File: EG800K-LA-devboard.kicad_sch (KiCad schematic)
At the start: 37 parts, among them J1 U.FL-R-SMT_10_, J2 MICROQTJ, J4 Conn_01x11_Pin, Q1 DTC143ZUAT106, Q2 DTC143ZUAT106, Q4 DTC143ZUAT106, Q5 DTC143ZUAT106, U1 EG800KEULC-I03-SNNSA

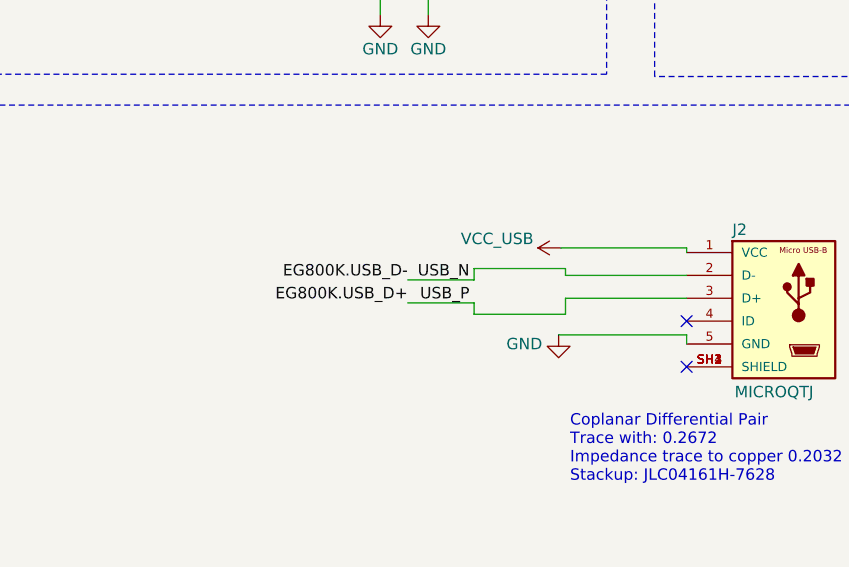
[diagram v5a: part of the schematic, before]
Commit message: Agregados res en serie en USB
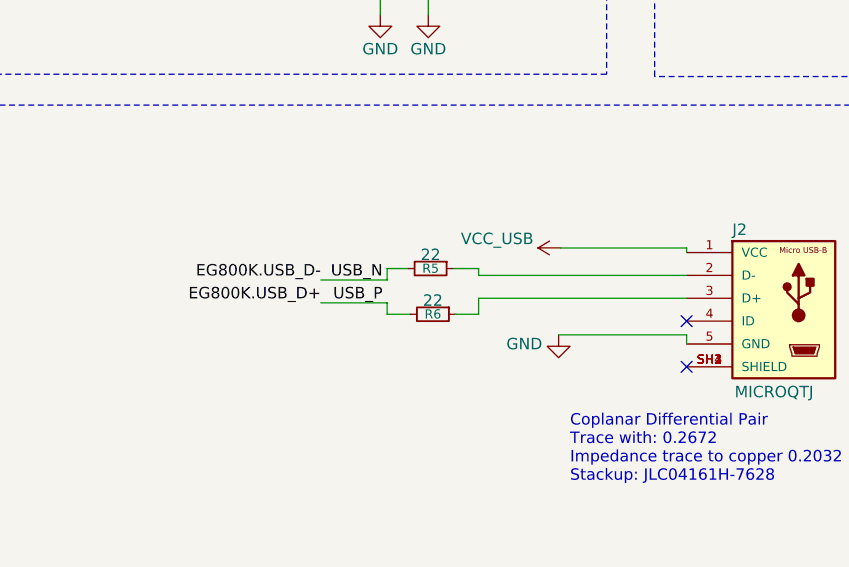
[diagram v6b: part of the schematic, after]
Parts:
- added R5, R6: 22, Resistor_SMD:R_0201_0603Metric_Pad0.64x0.40mm_HandSolder, symbol Device:R_Small
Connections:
- net EG800K.USB_D+: now also R6.2; no longer J2.3 (D+)
- net EG800K.USB_D-: now also R5.2; no longer J2.2 (D-)
- new net: J2.2 (D-), R5.1
- new net: J2.3 (D+), R6.1
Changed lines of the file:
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@@
 	(wire
 		(pts
-			(xy 105.664 174.752) (xy 119.126 174.752)
+			(xy 96.012 174.752) (xy 119.126 174.752)
 		)
 		(stroke
@@
 	(wire
 		(pts
-			(xy 88.138 175.26) (xy 95.504 175.26)
+			(xy 78.486 175.26) (xy 85.852 175.26)
 		)
 		(stroke
@@
 	(wire
 		(pts
-			(xy 95.504 177.8) (xy 95.504 179.07)
+			(xy 85.852 177.8) (xy 85.852 179.07)
 		)
 		(stroke
@@
 	(wire
 		(pts
-			(xy 88.138 177.8) (xy 95.504 177.8)
+			(xy 78.486 177.8) (xy 85.852 177.8)
 		)
 		(stroke
@@
 	(wire
 		(pts
-			(xy 95.504 175.26) (xy 95.504 173.99)
+			(xy 85.852 175.26) (xy 85.852 173.99)
 		)
 		(stroke
@@
 	(wire
 		(pts
-			(xy 95.504 179.07) (xy 105.664 179.07)
+			(xy 85.852 179.07) (xy 88.392 179.07)
 		)
 		(stroke
@@
 	(wire
 		(pts
+			(xy 93.218 173.99) (xy 96.012 173.99)
+		)
+		(stroke
+			(width 0)
+			(type default)
+		)
+	)
+	(wire
+		(pts
 			(xy 271.78 76.454) (xy 269.24 76.454)
 		)
@@
 	(wire
 		(pts
-			(xy 95.504 173.99) (xy 105.664 173.99)
+			(xy 85.852 173.99) (xy 88.138 173.99)
 		)
 		(stroke
@@
 	(wire
 		(pts
-			(xy 105.664 179.07) (xy 105.664 177.292)
+			(xy 96.012 179.07) (xy 96.012 177.292)
 		)
 		(stroke
@@
 	(wire
 		(pts
-			(xy 105.664 173.99) (xy 105.664 174.752)
+			(xy 96.012 173.99) (xy 96.012 174.752)
 		)
 		(stroke
@@
 	(wire
 		(pts
-			(xy 105.664 177.292) (xy 119.126 177.292)
+			(xy 96.012 177.292) (xy 119.126 177.292)
 		)
 		(stroke
@@
 	(wire
 		(pts
+			(xy 93.472 179.07) (xy 96.012 179.07)
+		)
+		(stroke
+			(width 0)
+			(type default)
+		)
+	)
+	(wire
+		(pts
 			(xy 39.624 272.288) (xy 53.086 272.288)
 		)
@@
 	)
 	(label "USB_N"
-		(at 94.996 175.26 180)
+		(at 85.344 175.26 180)
 		(effects
 			(font
@@
 	)
 	(label "USB_P"
-		(at 94.996 177.8 180)
+		(at 85.344 177.8 180)
 		(effects
 			(font
@@
 	)
 	(label "EG800K.USB_D+"
-		(at 88.138 177.8 180)
+		(at 78.486 177.8 180)
 		(effects
 			(font
@@
 	)
 	(label "EG800K.USB_D-"
-		(at 88.138 175.26 180)
+		(at 78.486 175.26 180)
 		(effects
 			(font
@@
 					(unit 1)
 				)
+			)
+		)
+	)
+	(symbol
+		(lib_name "R_Small_1")
+		(lib_id "Device:R_Small")
+		(at 90.932 179.07 270)
+		(unit 1)
+		(exclude_from_sim no)
+		(in_bom yes)
+		(on_board yes)
+		(dnp no)
+		(property "Reference" "R6"
+			(at 90.932 179.07 90)
+			(effects
+				(font
+					(size 1.016 1.016)
+				)
+			)
+		)
+		(property "Value" "22"
+			(at 90.932 177.546 90)
+			(effects
+				(font
+					(size 1.27 1.27)
+				)
+			)
+		)
+		(property "Footprint" "Resistor_SMD:R_0201_0603Metric_Pad0.64x0.40mm_HandSolder"
+			(at 90.932 179.07 0)
+			(effects
+				(font
+					(size 1.27 1.27)
+				)
+				(hide yes)
+			)
+		)
+		(property "Datasheet" "~"
+			(at 90.932 179.07 0)
+			(effects
+				(font
+					(size 1.27 1.27)
+				)
+				(hide yes)
+			)
+		)
+		(property "Description" "Resistor, small symbol"
+			(at 90.932 179.07 0)
+			(effects
+				(font
+					(size 1.27 1.27)
+				)
+				(hide yes)
+			)
+		)
+		(pin "1"
+		)
+		(pin "2"
+		)
+		(instances
+			(project "EG800K-LA-devboard"
+				(path "/1dd4973b-ee9b-455c-8ac7-91801682b6f0"
+					(reference "R6")
+					(unit 1)
+				)
+			)
+		)
+	)
+	(symbol
+		(lib_name "R_Small_1")
+		(lib_id "Device:R_Small")
+		(at 90.678 173.99 270)
+		(unit 1)
+		(exclude_from_sim no)
+		(in_bom yes)
+		(on_board yes)
+		(dnp no)
+		(property "Reference" "R5"
+			(at 90.678 173.99 90)
+			(effects
+				(font
+					(size 1.016 1.016)
+				)
+			)
+		)
+		(property "Value" "22"
+			(at 90.678 172.466 90)
+			(effects
+				(font
+					(size 1.27 1.27)
+				)
+			)
+		)
+		(property "Footprint" "Resistor_SMD:R_0201_0603Metric_Pad0.64x0.40mm_HandSolder"
+			(at 90.678 173.99 0)
+			(effects
+				(font
+					(size 1.27 1.27)
+				)
+				(hide yes)
+			)
+		)
+		(property "Datasheet" "~"
+			(at 90.678 173.99 0)
+			(effects
+				(font
+					(size 1.27 1.27)
+				)
+				(hide yes)
+			)
+		)
+		(property "Description" "Resistor, small symbol"
+			(at 90.678 173.99 0)
+			(effects
+				(font
+					(size 1.27 1.27)
+				)
+				(hide yes)
+			)
+		)
+		(pin "1"
+		)
+		(pin "2"
+		)
+		(instances
+			(project ""
+				(path "/1dd4973b-ee9b-455c-8ac7-91801682b6f0"
+					(reference "R5")
+					(unit 1)
+				)
